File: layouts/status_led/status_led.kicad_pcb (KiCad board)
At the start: 2 copper layers, 2 parts

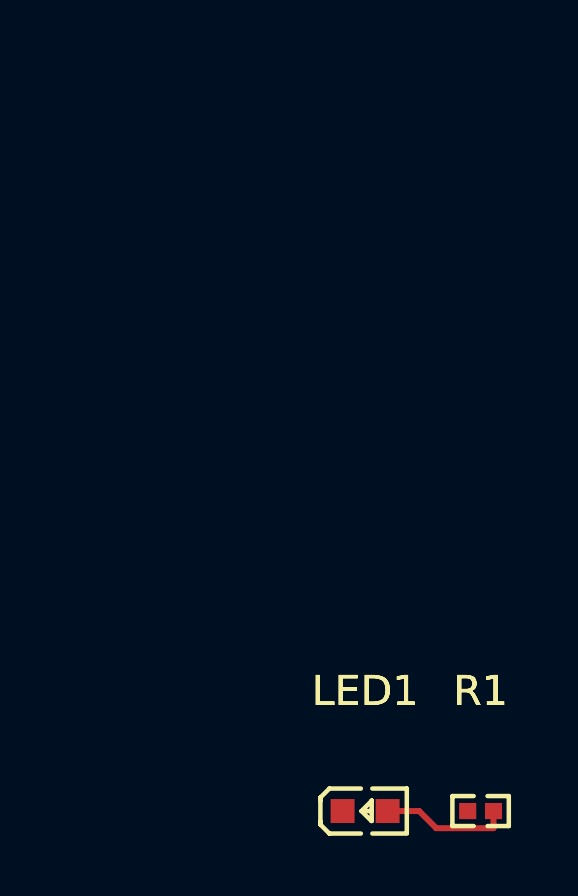
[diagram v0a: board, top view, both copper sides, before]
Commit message: Enhance smart placer with simulated annealing and pre-routing validation
Smart Placer improvements:
- Add simulated annealing refinement (now default) for better wire length optimization
- Add force-directed refinement with improvement safeguard
- Add silkscreen text repositioning to avoid component overlaps
- Significant wire length reductions (e.g., power_filter: 113mm -> 46mm)

Autorouter improvements:
- Add PreRoutingValidator class for pre-flight checks
- Validate unconnected pads, overlapping footprints, unplaced components
- Use pad-based bounds for accurate overlap detection
- Block routing on validation errors with actionable messages

Research:
- Add comprehensive autorouting/autoplacement findings document
- Cover Freerouting Python client, OrthoRoute, DeepPCB, KiCad 9 IPC API
- Document force-directed and simulated annealing algorithms

Cleanup:
- Update .gitignore for DSN/SES files, build artifacts, tools
- Remove stale timestamped build files
- Add parts footprints and symbols

All 10 modules placed and routed successfully.

Co-Authored-By: Claude Opus 4.5 <noreply@anthropic.com>
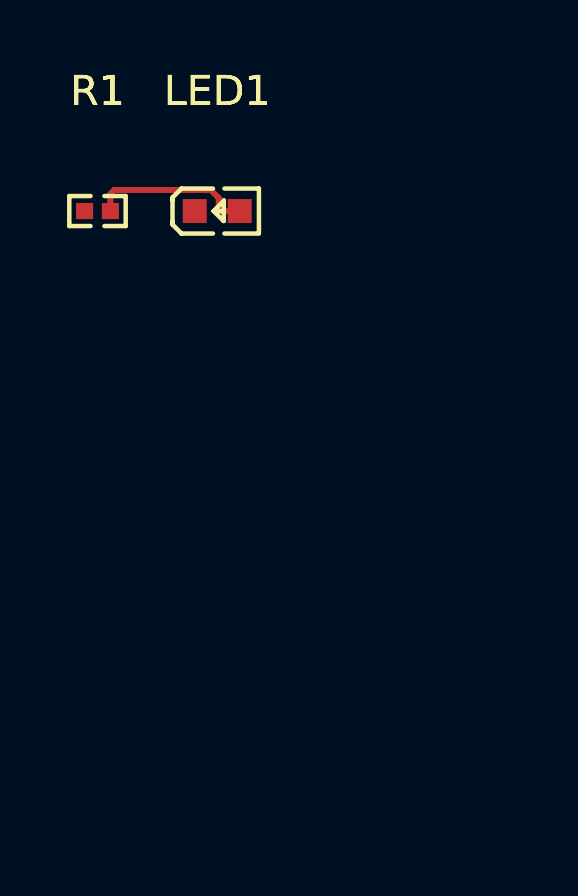
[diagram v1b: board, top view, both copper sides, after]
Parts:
- moved R1 23.7 mm to (87.2, 80.0)
- moved LED1 20.6 mm to (91.2, 80.0)
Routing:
- net A: track 3.99 -> 5.48 mm
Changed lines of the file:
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@@
 	(footprint "UNI_ROYAL_0402WGF1001TCE:R0402"
 		(layer "F.Cu")
-		(at 100 100)
+		(at 87.23 80)
 		(property "Reference" "R1"
 			(at 0 -4 0)
@@
 	(footprint "Everlight_Elec_19_217_GHC_YR1S2_3T:LED0603-RD"
 		(layer "F.Cu")
-		(at 96.15 100)
+		(at 91.2206 80)
 		(property "Reference" "LED1"
 			(at 0 -4 0)
@@
 	)
 	(segment
-		(start 97.25 100)
-		(end 97.9517 100)
+		(start 91.0058 79.2983)
+		(end 87.79 79.2983)
 		(width 0.2)
 		(layer "F.Cu")
@@
 	)
 	(segment
-		(start 97.9517 100)
-		(end 98.5234 100.5717)
+		(start 91.2689 80)
+		(end 91.2689 79.5614)
 		(width 0.2)
 		(layer "F.Cu")
@@
 	)
 	(segment
-		(start 98.5234 100.5717)
-		(end 100.43 100.5717)
+		(start 91.2689 79.5614)
+		(end 91.0058 79.2983)
 		(width 0.2)
 		(layer "F.Cu")
@@
 	)
 	(segment
-		(start 100.43 100)
-		(end 100.43 100.5717)
+		(start 87.79 79.2983)
+		(end 87.66 79.4283)
 		(width 0.2)
 		(layer "F.Cu")
+		(net 1)
+	)
+	(segment
+		(start 87.66 80)
+		(end 87.66 79.4283)
+		(width 0.2)
+		(layer "F.Cu")
+		(net 1)
+	)
+	(segment
+		(start 91.9706 80)
+		(end 91.2689 80)
+		(width 0.2)
+		(layer "F.Cu")
